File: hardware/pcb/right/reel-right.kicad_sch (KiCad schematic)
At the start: 43 parts, among them J1 Conn_01x02, J3 Conn_01x05, SW1 SW_Push, SW10 SW_Push, SW11 SW_Push, SW12 SW_Push, SW13 SW_Push, SW14 SW_Push, SW15 SW_Push, SW16 SW_Push, SW17 SW_Push, SW18 SW_Push, SW19 SW_Push, SW2 SW_Push, SW22 SW_SPDT, SW3 SW_Push, SW4 SW_Push, SW5 SW_Push, SW6 SW_Push, SW7 SW_Push, SW8 SW_Push, SW9 SW_Push

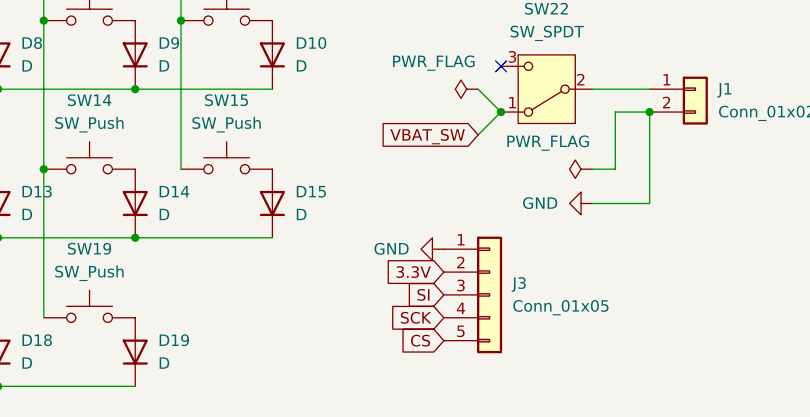
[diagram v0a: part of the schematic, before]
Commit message: Correct ReeL PCB connector pinouts and routing
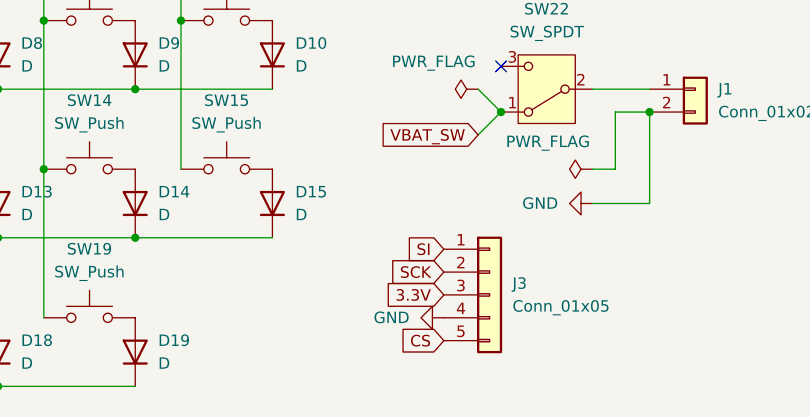
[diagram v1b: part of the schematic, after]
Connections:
- net 3.3V: now also J3.3 (Pin_3); no longer J3.2 (Pin_2)
- net GND: now also J3.4 (Pin_4); no longer J3.1 (Pin_1)
- net SCK: now also J3.2 (Pin_2); no longer J3.4 (Pin_4)
- net SI: now also J3.1 (Pin_1); no longer J3.3 (Pin_3)
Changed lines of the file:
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@@
 	(global_label "SI"
 		(shape input)
-		(at 121.92 152.4 180)
+		(at 121.92 147.32 180)
 		(fields_autoplaced yes)
 		(effects
@@
 		)
 		(property "Intersheetrefs" "${INTERSHEET_REFS}"
-			(at 117.1205 152.4 0)
+			(at 117.1205 147.32 0)
 			(hide yes)
 			(show_name no)
@@
 	(global_label "SCK"
 		(shape input)
-		(at 121.92 154.94 180)
+		(at 121.92 149.86 180)
 		(fields_autoplaced yes)
 		(effects
@@
 		)
 		(property "Intersheetrefs" "${INTERSHEET_REFS}"
-			(at 115.1853 154.94 0)
+			(at 115.1853 149.86 0)
 			(hide yes)
 			(show_name no)
@@
 	(global_label "3.3V"
 		(shape input)
-		(at 121.92 149.86 180)
+		(at 121.92 152.4 180)
 		(fields_autoplaced yes)
 		(effects
@@
 		)
 		(property "Intersheetrefs" "${INTERSHEET_REFS}"
-			(at 114.8224 149.86 0)
+			(at 114.8224 152.4 0)
 			(hide yes)
 			(show_name no)
@@
 	(symbol
 		(lib_id "power:GND")
-		(at 121.92 147.32 270)
+		(at 121.92 154.94 270)
 		(unit 1)
 		(body_style 1)
@@
 		(fields_autoplaced yes)
 		(property "Reference" "#PWR03"
-			(at 115.57 147.32 0)
+			(at 115.57 154.94 0)
 			(hide yes)
 			(show_name no)
@@
 		)
 		(property "Value" "GND"
-			(at 118.11 147.3199 90)
+			(at 118.11 154.9399 90)
 			(show_name no)
 			(do_not_autoplace no)
@@
 		)
 		(property "Footprint" ""
-			(at 121.92 147.32 0)
+			(at 121.92 154.94 0)
 			(hide yes)
 			(show_name no)
@@
 		)
 		(property "Datasheet" ""
-			(at 121.92 147.32 0)
+			(at 121.92 154.94 0)
 			(hide yes)
 			(show_name no)
@@
 		)
 		(property "Description" "Power symbol creates a global label with name \"GND\" , ground"
-			(at 121.92 147.32 0)
+			(at 121.92 154.94 0)
 			(hide yes)
 			(show_name no)
